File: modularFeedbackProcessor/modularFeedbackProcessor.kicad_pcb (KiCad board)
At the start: 2 copper layers, 191.5 x 124 mm, 203 parts, among them J1 Input, J10 Output, J2 Feedback, J4 Eurorack_Power_16pin_Unshroud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, J5 DryWet, J6 Rate, J7 EffectsRouteIn, J8 EffectsRouteOut, J9 EffectsDryWet, Q1 Q_PMOS_GDS, Q10 Q_PMOS_GDS, Q11 Q_NMOS_GDS, Q12 Q_PMOS_GDS, Q13 Q_PMOS_GDS, Q14 Q_NMOS_GDS, Q15 Q_PMOS_GDS, Q16 Q_NMOS_GDS, Q17 Q_PMOS_GDS, Q18 Q_NMOS_GDS, Q19 Q_PMOS_GDS, Q2 Q_NMOS_GDS, Q3 Q_PMOS_GDS, Q4 Q_PMOS_GDS, Q5 Q_NMOS_GDS, Q6 Q_PMOS_GDS, Q7 Q_NMOS_GDS, Q8 Q_PMOS_GDS, Q9 Q_NMOS_GDS, SW1 EffectsRouting, U1 TL074, U10 LM13700, U2 TL074, U3 LM13700, U4 V3205, U5 CD4046, U6 LF398_DIP8, U7 TL074, U8 LM13700, U9 TL074

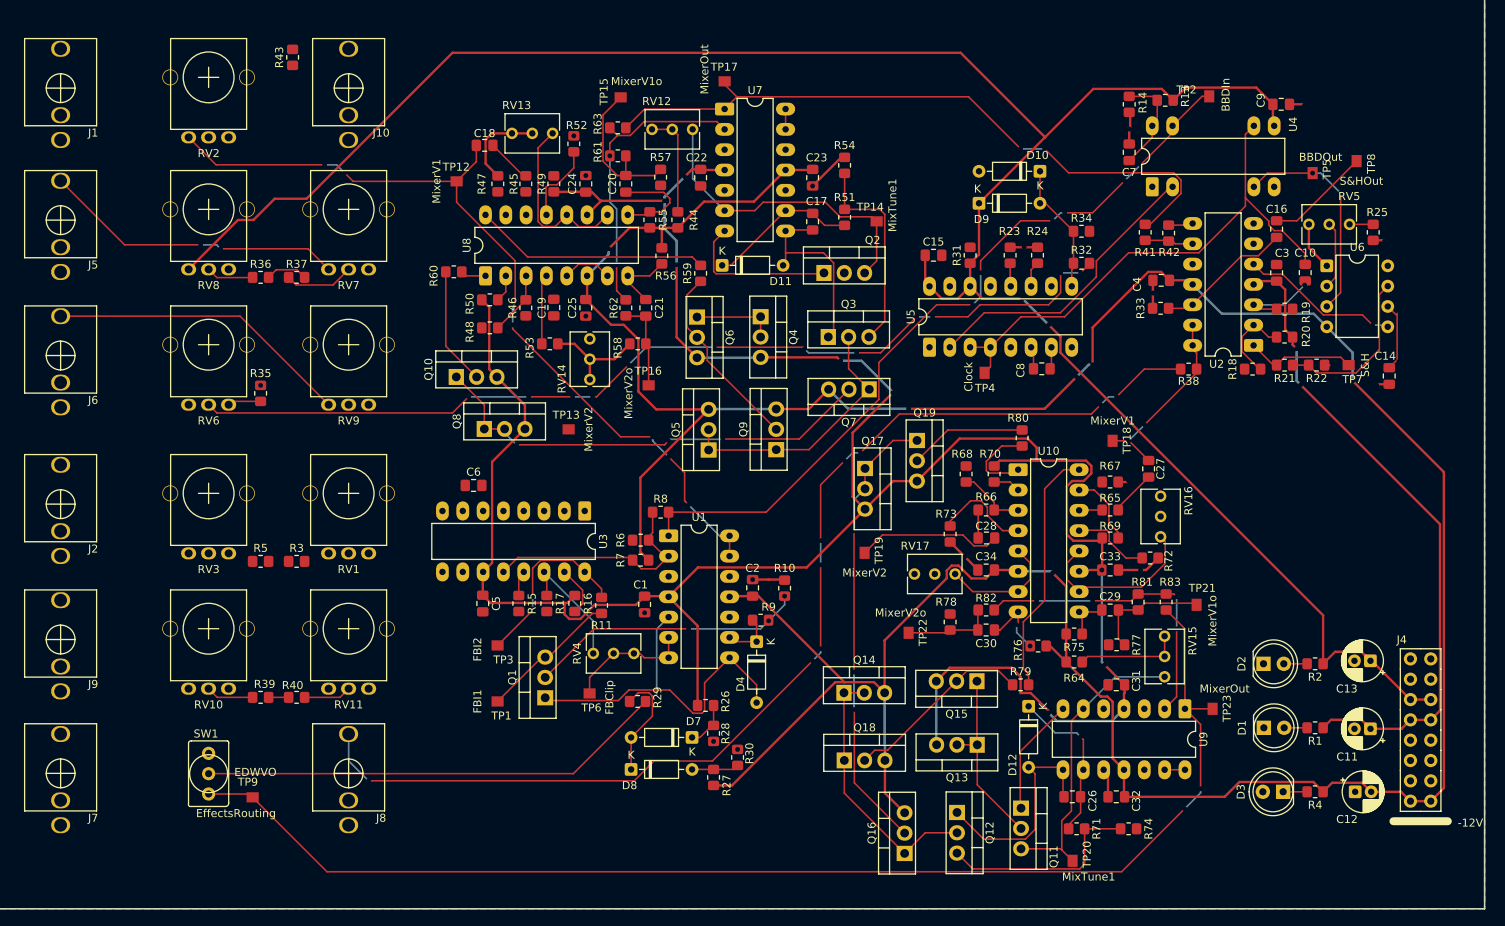
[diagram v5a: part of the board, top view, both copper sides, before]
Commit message: first version to pass DRC
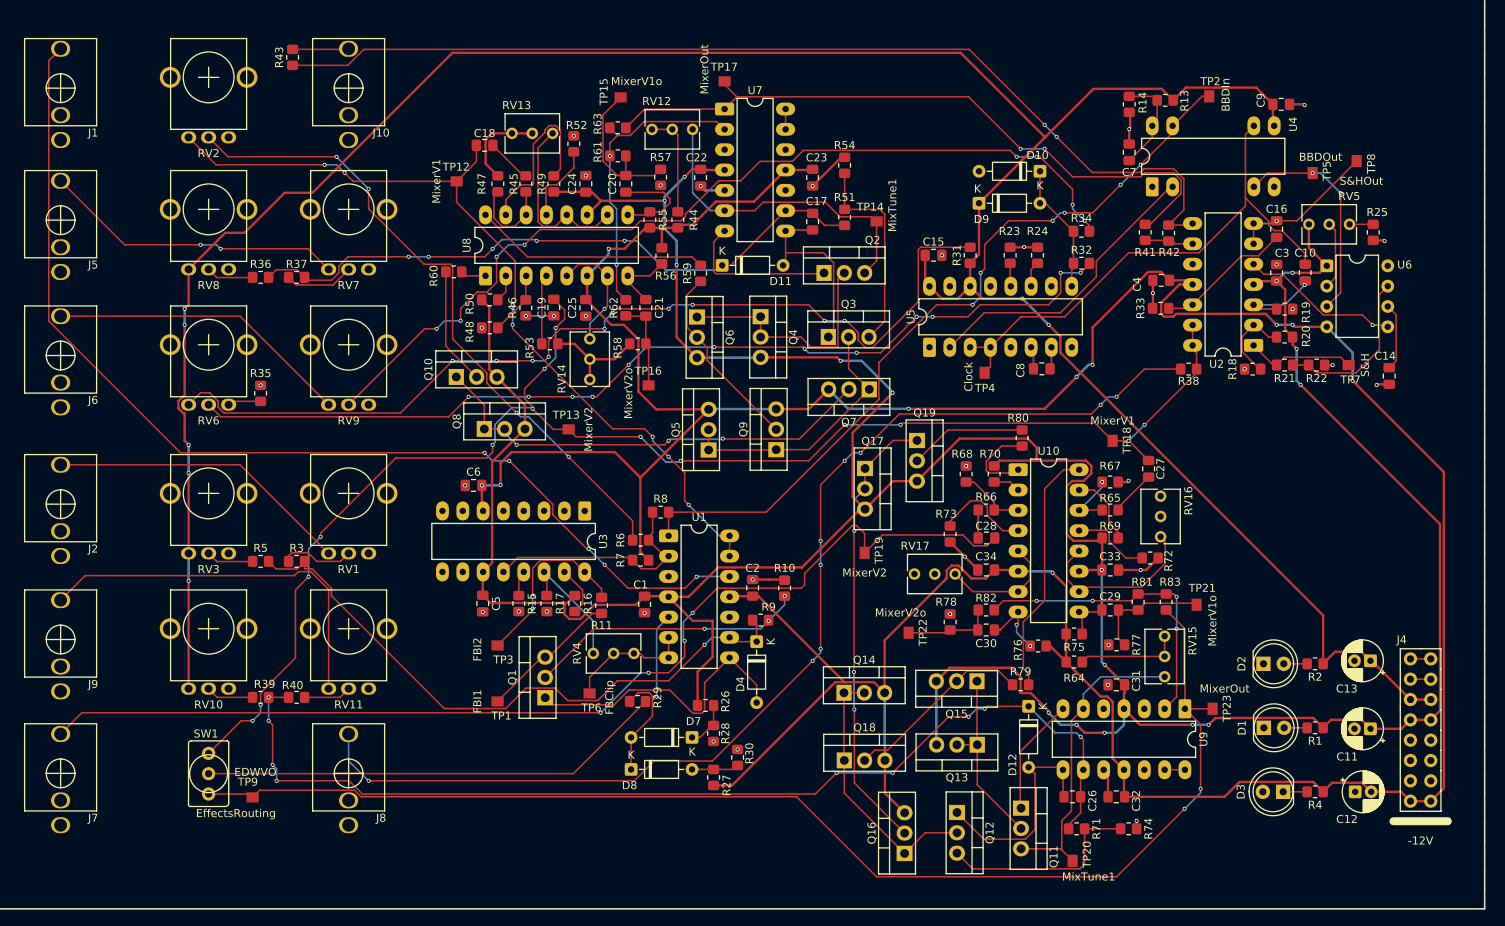
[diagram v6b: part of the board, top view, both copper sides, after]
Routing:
- net /Mixer1/V_{in2}: track 23.7 -> 187.7 mm, vias 2 -> 14
- net /in: track 0.00 -> 134.9 mm, vias 0 -> 5
- net Net-(R42-Pad2): track 3.08 -> 129.0 mm, vias 0 -> 2
- net Net-(R31-Pad2): track 0.00 -> 118.9 mm, vias 0 -> 10
- net /Mixer2/V_{in2}: track 18.2 -> 135.9 mm, vias 0 -> 4
- net Net-(R34-Pad2): track 0.00 -> 114.7 mm, vias 0 -> 8
- net /Mixer2/V_{ctrl}: track 23.0 -> 133.0 mm, vias 1 -> 9
- net Net-(R6-Pad1): track 0.00 -> 82.8 mm, vias 0 -> 4
- net Net-(D4-K): track 6.50 -> 78.6 mm, vias 0 -> 1
- net /Mixer1/V_{ctrl}: track 24.2 -> 80.9 mm, vias 0 -> 5
- net +5V: track 276.0 -> 330.1 mm, vias 2 -> 7
- net Net-(J9-T): track 0.00 -> 48.3 mm
- net +12V: track 410.3 -> 449.4 mm, vias 10 -> 16
- net Net-(J2-T): track 0.00 -> 38.1 mm
- net -12V: track 417.3 -> 454.0 mm, vias 6 -> 10
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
